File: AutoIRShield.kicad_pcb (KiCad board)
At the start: 2 copper layers, 85.1 x 53.3 mm, 17 parts, among them P1 Power, P2 Analog, P3 Digital, P4 Digital, Q1 2SK4017, SW1 2MS1-T1-B4-VS2-Q-E-S, SW2 EC12E2420801, U1 ATD1602CPB, U2 RTC_DS3231, U3 IRReceiver_OSRB38C9AA

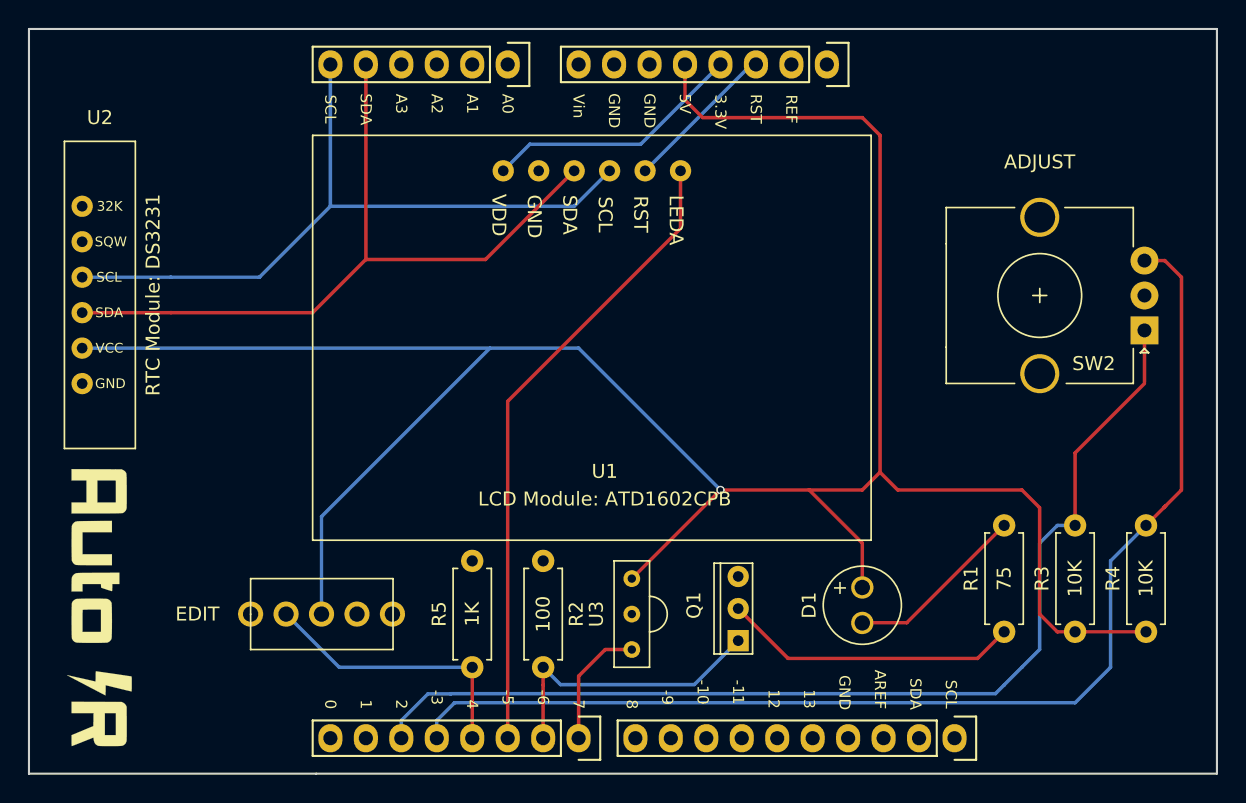
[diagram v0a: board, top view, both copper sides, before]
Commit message: 電源ラインの幅を太くして自動配線
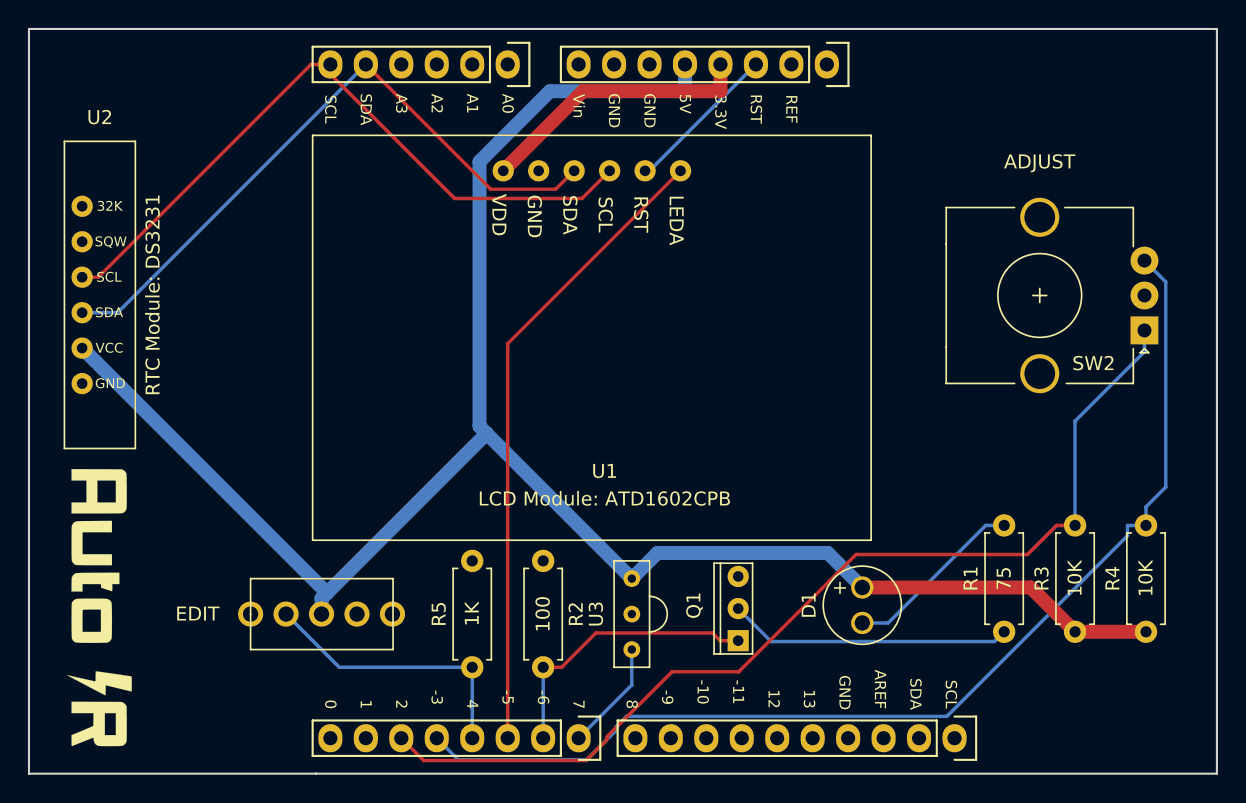
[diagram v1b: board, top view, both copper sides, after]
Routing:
- net +5V: track 173.4 -> 135.7 mm, vias 1 -> 0
- net /A4(SDA): track 53.4 -> 46.8 mm
- net /3(**): track 84.5 -> 79.2 mm
- net /2: track 75.7 -> 72.0 mm
- net /A5(SCL): track 51.1 -> 49.6 mm
- net +3V3: track 18.7 -> 19.8 mm
- net /7: track 9.04 -> 7.93 mm
- net Net-(Q1-Pad2): track 21.3 -> 20.3 mm
- net /6(**): track 21.3 -> 20.3 mm
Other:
- net class Power added: clearance 0.4, trace_width 1, via_dia 0.6, via_drill 0.4
